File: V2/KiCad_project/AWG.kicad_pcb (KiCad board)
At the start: 4 copper layers, 58 x 77.4 mm, 208 parts, among them J101 BNC_Amphenol_ICC 031-5329-51R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, Q201 MMBT3906, Q202 BC846B, Q301 MMBT3906, Q401 BC846B, Q402 BC846B, Q403 BC846B, Q404 BC846B, Q405 BC846B, U301 OPA2673IRGVR, U303 NE5532DR, U501 LM393DR2G, X1 Conn_02x20_1.27mm_SMD_Header_M, X2 Conn_02x05_1.27mm_SMD_Header_M

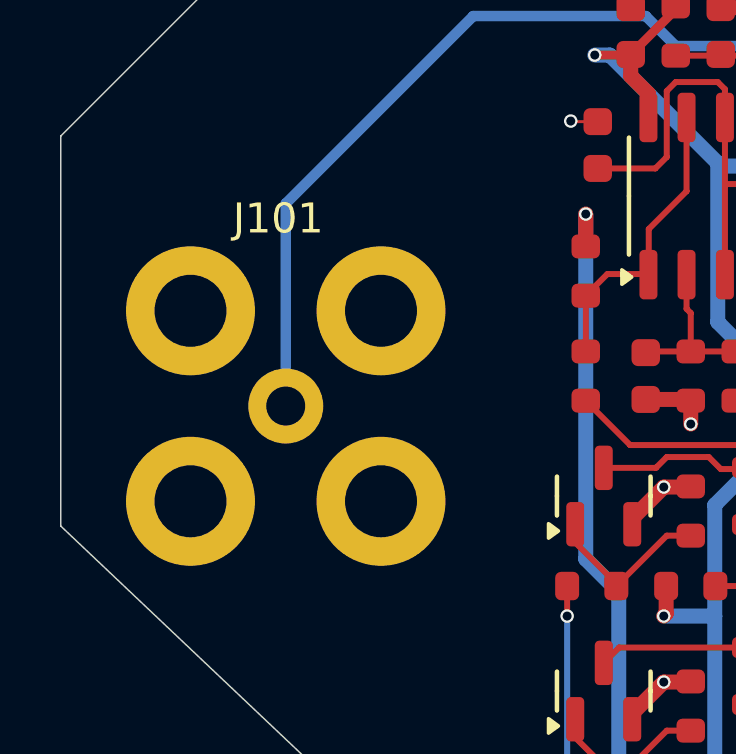
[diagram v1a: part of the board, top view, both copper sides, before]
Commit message: Silkscreen convenience improvements
* show BNC lug orientation
* label connectors on bottom layer
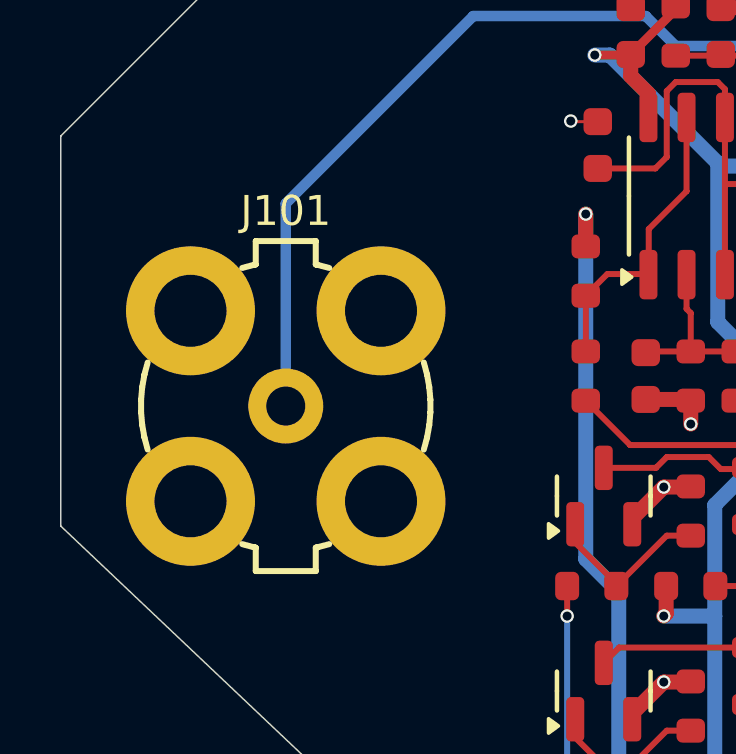
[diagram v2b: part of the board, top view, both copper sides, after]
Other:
- board text added: "OUT"
- board text added: "PROT"

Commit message: Added ordering number to value of U201, U202 and U302 because it did not appear in schematic.pdf and in bom.csv
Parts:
- U201, U202: value ~ -> LMR54406FDBVR
- U302: value ~ -> AD9744ACPZRL7
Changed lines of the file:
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@@
 			)
 		)
-		(property "Value" "~"
+		(property "Value" "LMR54406FDBVR"
 			(at 0 2.4 90)
 			(layer "F.Fab")
@@
 			)
 		)
-		(property "Value" "~"
+		(property "Value" "AD9744ACPZRL7"
 			(at 0 4.002 0)
 			(layer "F.Fab")
@@
 			)
 		)
-		(property "Value" "~"
+		(property "Value" "LMR54406FDBVR"
 			(at 0 2.4 0)
 			(layer "F.Fab")
